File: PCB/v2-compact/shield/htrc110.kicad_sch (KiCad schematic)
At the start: 0 parts

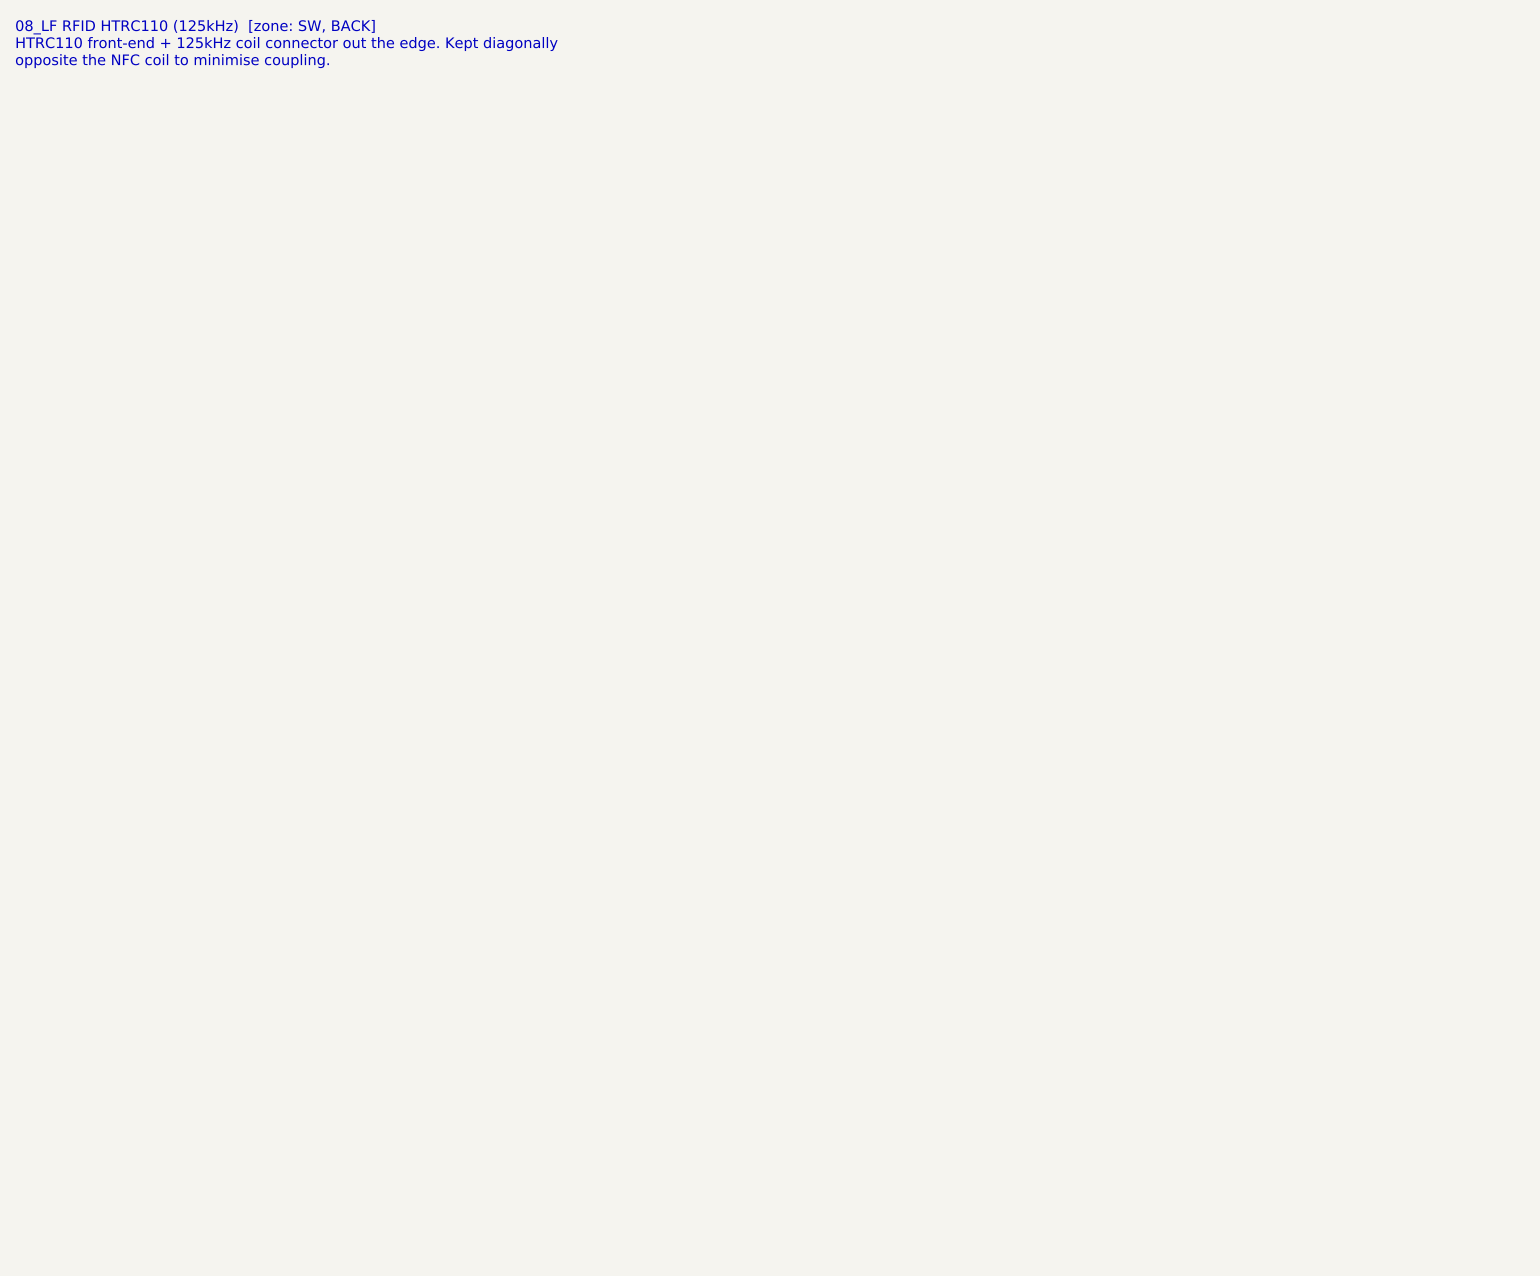
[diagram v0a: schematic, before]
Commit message: Schematics: HTRC110 and RV1106 sheets — full sheet set complete
- 08_LF_RFID_HTRC110: 5V HITAG reader, 3-wire (SCLK/DIN/DOUT) to the C5, DOUT
  open-drain pulled to 3.3V, 4MHz crystal, decoupling. LF coil tank flagged;
  pins 8-14 flagged to verify against the datasheet.
- 04_RV1106_Linux (A3): Core1106 SoM self-powered from its own USB-C (CC
  resistors) with its own microSD; UART to the S3 over J1 (RV_TX/RX/CTRL).
  Symbol is functional with placeholder pin numbers, flagged to verify against
  the Luckfox pinout.
- Add HTRC110 + RV1106 custom symbols to SnowOwl.kicad_sym.

All 17 sheets across both boards are now captured and netlist-verified
(153 nets). Remaining: ERC cleanup (no-connects + power flags), the two flagged
pinouts, RF matching values, and finishing the module footprints.
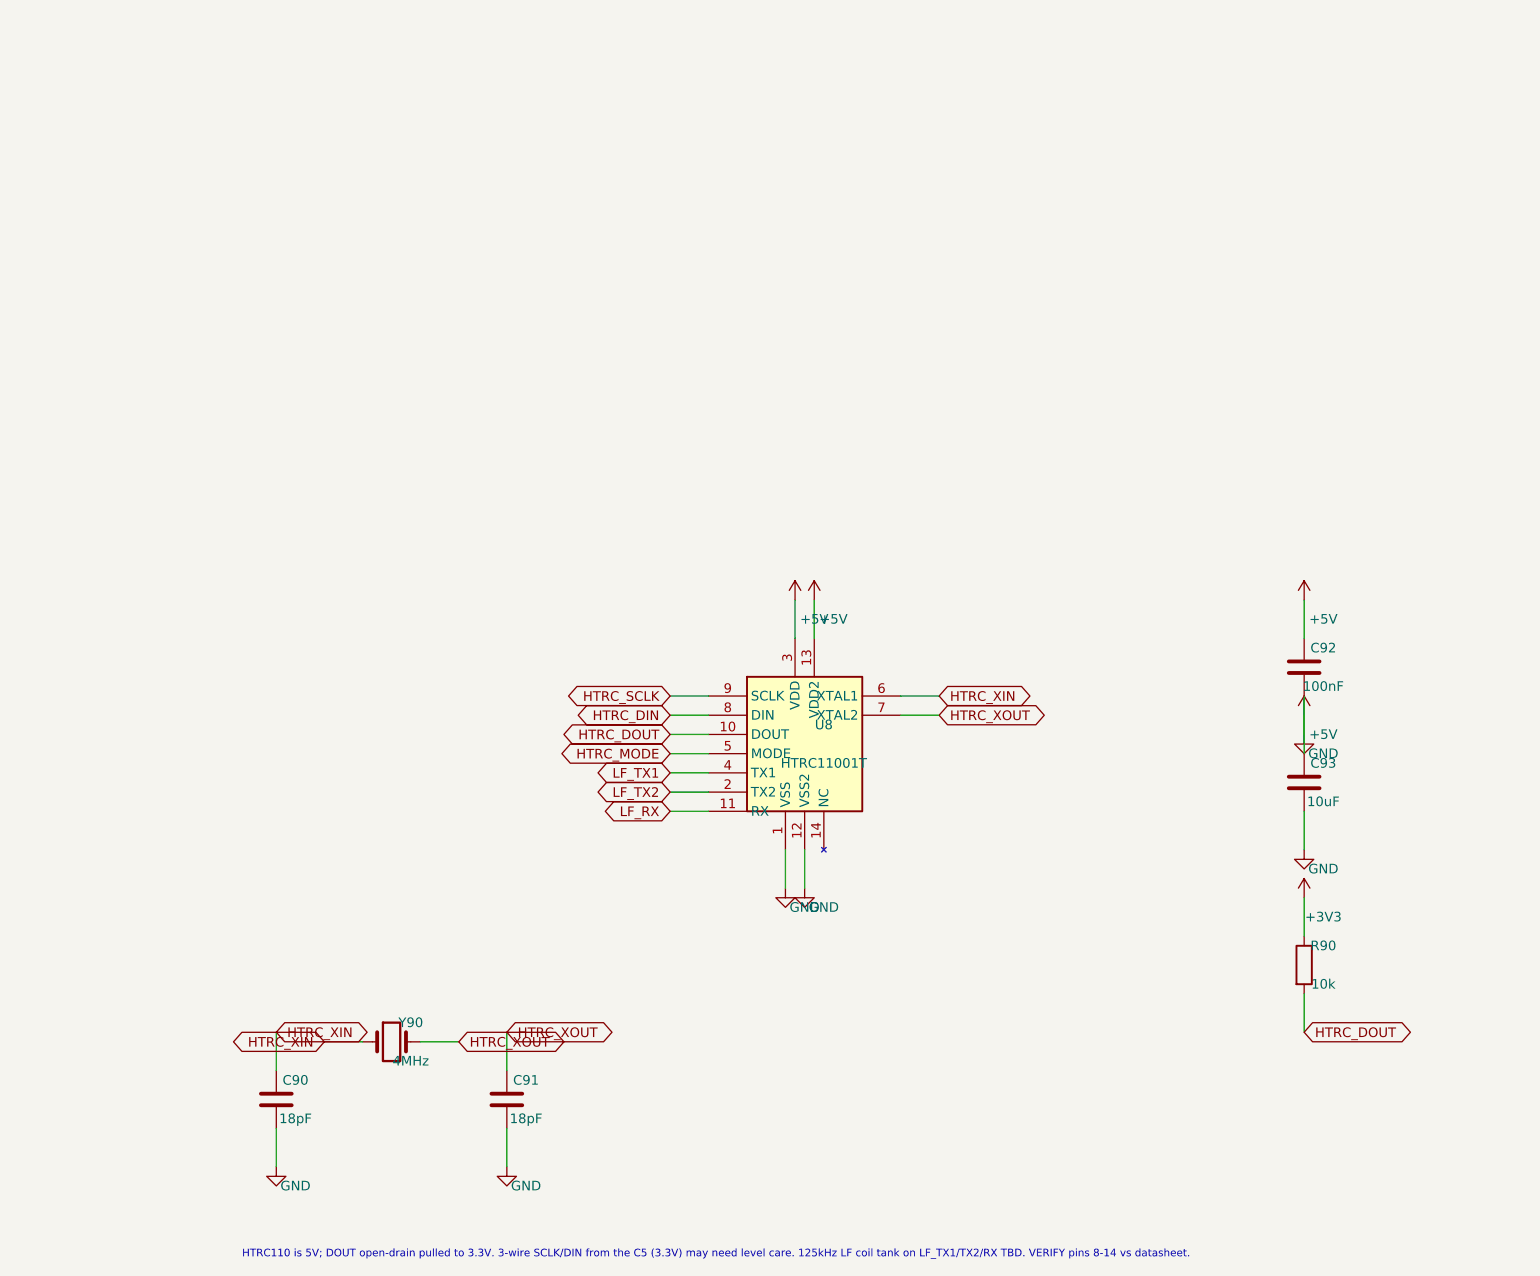
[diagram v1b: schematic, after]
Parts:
- added C90, C91: 18pF, Capacitor_SMD:C_0402_1005Metric, symbol Device:C
- added C92: 100nF, Capacitor_SMD:C_0402_1005Metric, symbol Device:C
- added C93: 10uF, Capacitor_SMD:C_0402_1005Metric, symbol Device:C
- added R90: 10k, Resistor_SMD:R_0402_1005Metric, symbol Device:R
- added U8: HTRC11001T, Package_SO:SO-14_3.9x8.7mm_P1.27mm, symbol SnowOwl:HTRC110
- added Y90: 4MHz, Crystal:Crystal_SMD_3225-4Pin_3.2x2.5mm, symbol Device:Crystal
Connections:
- new net +3V3: R90.1
- new net +5V: C90.2, C91.2, C92.1, C92.2, C93.1, C93.2, U8.1 (VSS), U8.12 (VSS2), U8.13 (VDD2), U8.3 (VDD)
- new net HTRC_DIN: U8.8 (DIN)
- new net HTRC_DOUT: R90.2, U8.10 (DOUT)
- new net HTRC_MODE: U8.5 (MODE)
- new net HTRC_SCLK: U8.9 (SCLK)
- new net HTRC_XIN: C90.1, U8.6 (XTAL1), Y90.1
- new net HTRC_XOUT: C91.1, U8.7 (XTAL2), Y90.2
- new net LF_RX: U8.11 (RX)
- new net LF_TX1: U8.4 (TX1)
- new net LF_TX2: U8.2 (TX2)
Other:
- note added: "HTRC110 is 5V; DOUT open-drain pulled to 3.3V. 3-wire SCLK/DIN from the C5 (3.3V) may need level care. 125kHz LF coil tank on LF_TX1/TX2/RX TBD. VERIFY pins 8-14 vs datasheet."
- note removed: "08_LF RFID HTRC110 (125kHz) [zone: SW, BACK] HTRC110 front-end + 125kHz coil connector out the edge. Kept diagonally opposite the NFC coil to minimise coupling."

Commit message: Schematics: cleanup - HTRC110 footprint (SOIC-14), reset pull-ups (CC1200/GPS), RV1106 power flags
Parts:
- U8: footprint Package_SO:SO-14_3.9x8.7mm_P1.27mm -> Package_SO:SOIC-14_3.9x8.7mm_P1.27mm
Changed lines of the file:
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@@
     (property "Reference" "U8" (at 121.92 107.95 0) (effects (font (size 1.27 1.27))))
     (property "Value" "HTRC11001T" (at 121.92 113.03 0) (effects (font (size 1.27 1.27))))
-    (property "Footprint" "Package_SO:SO-14_3.9x8.7mm_P1.27mm" (at 119.38 110.49 0) (effects (font (size 1.27 1.27)) hide))
+    (property "Footprint" "Package_SO:SOIC-14_3.9x8.7mm_P1.27mm" (at 119.38 110.49 0) (effects (font (size 1.27 1.27)) hide))
     (pin "9")
     (pin "8")
@@
   (symbol (lib_id "power:+5V") (at 118.11 91.44 0) (unit 1)
     (in_bom yes) (on_board yes) (dnp no)
-    (property "Reference" "#PWRF84A393" (at 120.65 88.9 0) (effects (font (size 1.27 1.27)) hide))
+    (property "Reference" "#PWR57BC623" (at 120.65 88.9 0) (effects (font (size 1.27 1.27)) hide))
     (property "Value" "+5V" (at 120.65 93.98 0) (effects (font (size 1.27 1.27))))
     (property "Footprint" "" (at 118.11 91.44 0) (effects (font (size 1.27 1.27)) hide))
     (pin "1")
-    (instances (project "SnowOwl-Shield" (path "/44195f86-bade-400a-b1c6-65bd4a325d72" (reference "#PWRF84A393") (unit 1))))
+    (instances (project "SnowOwl-Shield" (path "/44195f86-bade-400a-b1c6-65bd4a325d72" (reference "#PWR57BC623") (unit 1))))
   )
   (wire (pts (xy 120.65 96.52) (xy 120.65 91.44)) (stroke (width 0) (type default)))
   (symbol (lib_id "power:+5V") (at 120.65 91.44 0) (unit 1)
     (in_bom yes) (on_board yes) (dnp no)
-    (property "Reference" "#PWR5422CC2" (at 123.19 88.9 0) (effects (font (size 1.27 1.27)) hide))
+    (property "Reference" "#PWR49814C8" (at 123.19 88.9 0) (effects (font (size 1.27 1.27)) hide))
     (property "Value" "+5V" (at 123.19 93.98 0) (effects (font (size 1.27 1.27))))
     (property "Footprint" "" (at 120.65 91.44 0) (effects (font (size 1.27 1.27)) hide))
     (pin "1")
-    (instances (project "SnowOwl-Shield" (path "/44195f86-bade-400a-b1c6-65bd4a325d72" (reference "#PWR5422CC2") (unit 1))))
+    (instances (project "SnowOwl-Shield" (path "/44195f86-bade-400a-b1c6-65bd4a325d72" (reference "#PWR49814C8") (unit 1))))
   )
   (wire (pts (xy 116.84 124.46) (xy 116.84 129.54)) (stroke (width 0) (type default)))
   (symbol (lib_id "power:GND") (at 116.84 129.54 0) (unit 1)
     (in_bom yes) (on_board yes) (dnp no)
-    (property "Reference" "#PWR7639A3B" (at 119.38 127 0) (effects (font (size 1.27 1.27)) hide))
+    (property "Reference" "#PWR3B37F8B" (at 119.38 127 0) (effects (font (size 1.27 1.27)) hide))
     (property "Value" "GND" (at 119.38 132.08 0) (effects (font (size 1.27 1.27))))
     (property "Footprint" "" (at 116.84 129.54 0) (effects (font (size 1.27 1.27)) hide))
     (pin "1")
-    (instances (project "SnowOwl-Shield" (path "/44195f86-bade-400a-b1c6-65bd4a325d72" (reference "#PWR7639A3B") (unit 1))))
+    (instances (project "SnowOwl-Shield" (path "/44195f86-bade-400a-b1c6-65bd4a325d72" (reference "#PWR3B37F8B") (unit 1))))
   )
   (wire (pts (xy 119.38 124.46) (xy 119.38 129.54)) (stroke (width 0) (type default)))
   (symbol (lib_id "power:GND") (at 119.38 129.54 0) (unit 1)
     (in_bom yes) (on_board yes) (dnp no)
-    (property "Reference" "#PWRC1F4483" (at 121.92 127 0) (effects (font (size 1.27 1.27)) hide))
+    (property "Reference" "#PWRA2B0F19" (at 121.92 127 0) (effects (font (size 1.27 1.27)) hide))
     (property "Value" "GND" (at 121.92 132.08 0) (effects (font (size 1.27 1.27))))
     (property "Footprint" "" (at 119.38 129.54 0) (effects (font (size 1.27 1.27)) hide))
     (pin "1")
-    (instances (project "SnowOwl-Shield" (path "/44195f86-bade-400a-b1c6-65bd4a325d72" (reference "#PWRC1F4483") (unit 1))))
+    (instances (project "SnowOwl-Shield" (path "/44195f86-bade-400a-b1c6-65bd4a325d72" (reference "#PWRA2B0F19") (unit 1))))
   )
   (symbol (lib_id "Device:Crystal") (at 64.77 149.86 0) (unit 1)
@@
   (symbol (lib_id "power:GND") (at 49.53 166.37 0) (unit 1)
     (in_bom yes) (on_board yes) (dnp no)
-    (property "Reference" "#PWR69757A2" (at 52.07 163.83 0) (effects (font (size 1.27 1.27)) hide))
+    (property "Reference" "#PWR4014A64" (at 52.07 163.83 0) (effects (font (size 1.27 1.27)) hide))
     (property "Value" "GND" (at 52.07 168.91 0) (effects (font (size 1.27 1.27))))
     (property "Footprint" "" (at 49.53 166.37 0) (effects (font (size 1.27 1.27)) hide))
     (pin "1")
-    (instances (project "SnowOwl-Shield" (path "/44195f86-bade-400a-b1c6-65bd4a325d72" (reference "#PWR69757A2") (unit 1))))
+    (instances (project "SnowOwl-Shield" (path "/44195f86-bade-400a-b1c6-65bd4a325d72" (reference "#PWR4014A64") (unit 1))))
   )
   (symbol (lib_id "Device:C") (at 80.01 157.48 0) (unit 1)
@@
   (symbol (lib_id "power:GND") (at 80.01 166.37 0) (unit 1)
     (in_bom yes) (on_board yes) (dnp no)
-    (property "Reference" "#PWRE258DD7" (at 82.55 163.83 0) (effects (font (size 1.27 1.27)) hide))
+    (property "Reference" "#PWR93BA09D" (at 82.55 163.83 0) (effects (font (size 1.27 1.27)) hide))
     (property "Value" "GND" (at 82.55 168.91 0) (effects (font (size 1.27 1.27))))
     (property "Footprint" "" (at 80.01 166.37 0) (effects (font (size 1.27 1.27)) hide))
     (pin "1")
-    (instances (project "SnowOwl-Shield" (path "/44195f86-bade-400a-b1c6-65bd4a325d72" (reference "#PWRE258DD7") (unit 1))))
+    (instances (project "SnowOwl-Shield" (path "/44195f86-bade-400a-b1c6-65bd4a325d72" (reference "#PWR93BA09D") (unit 1))))
   )
   (symbol (lib_id "Device:C") (at 185.42 100.33 0) (unit 1)
@@
   (symbol (lib_id "power:+5V") (at 185.42 91.44 0) (unit 1)
     (in_bom yes) (on_board yes) (dnp no)
-    (property "Reference" "#PWR30B3E4C" (at 187.96 88.9 0) (effects (font (size 1.27 1.27)) hide))
+    (property "Reference" "#PWR6CCB33C" (at 187.96 88.9 0) (effects (font (size 1.27 1.27)) hide))
     (property "Value" "+5V" (at 187.96 93.98 0) (effects (font (size 1.27 1.27))))
     (property "Footprint" "" (at 185.42 91.44 0) (effects (font (size 1.27 1.27)) hide))
     (pin "1")
-    (instances (project "SnowOwl-Shield" (path "/44195f86-bade-400a-b1c6-65bd4a325d72" (reference "#PWR30B3E4C") (unit 1))))
+    (instances (project "SnowOwl-Shield" (path "/44195f86-bade-400a-b1c6-65bd4a325d72" (reference "#PWR6CCB33C") (unit 1))))
   )
   (wire (pts (xy 185.42 104.14) (xy 185.42 109.22)) (stroke (width 0) (type default)))
   (symbol (lib_id "power:GND") (at 185.42 109.22 0) (unit 1)
     (in_bom yes) (on_board yes) (dnp no)
-    (property "Reference" "#PWR708FD7F" (at 187.96 106.68 0) (effects (font (size 1.27 1.27)) hide))
+    (property "Reference" "#PWRB0B70CD" (at 187.96 106.68 0) (effects (font (size 1.27 1.27)) hide))
     (property "Value" "GND" (at 187.96 111.76 0) (effects (font (size 1.27 1.27))))
     (property "Footprint" "" (at 185.42 109.22 0) (effects (font (size 1.27 1.27)) hide))
     (pin "1")
-    (instances (project "SnowOwl-Shield" (path "/44195f86-bade-400a-b1c6-65bd4a325d72" (reference "#PWR708FD7F") (unit 1))))
+    (instances (project "SnowOwl-Shield" (path "/44195f86-bade-400a-b1c6-65bd4a325d72" (reference "#PWRB0B70CD") (unit 1))))
   )
   (symbol (lib_id "Device:C") (at 185.42 115.57 0) (unit 1)
@@
   (symbol (lib_id "power:+5V") (at 185.42 106.68 0) (unit 1)
     (in_bom yes) (on_board yes) (dnp no)
-    (property "Reference" "#PWR9636F1C" (at 187.96 104.14 0) (effects (font (size 1.27 1.27)) hide))
+    (property "Reference" "#PWRE868CCD" (at 187.96 104.14 0) (effects (font (size 1.27 1.27)) hide))
     (property "Value" "+5V" (at 187.96 109.22 0) (effects (font (size 1.27 1.27))))
     (property "Footprint" "" (at 185.42 106.68 0) (effects (font (size 1.27 1.27)) hide))
     (pin "1")
-    (instances (project "SnowOwl-Shield" (path "/44195f86-bade-400a-b1c6-65bd4a325d72" (reference "#PWR9636F1C") (unit 1))))
+    (instances (project "SnowOwl-Shield" (path "/44195f86-bade-400a-b1c6-65bd4a325d72" (reference "#PWRE868CCD") (unit 1))))
   )
   (wire (pts (xy 185.42 119.38) (xy 185.42 124.46)) (stroke (width 0) (type default)))
   (symbol (lib_id "power:GND") (at 185.42 124.46 0) (unit 1)
     (in_bom yes) (on_board yes) (dnp no)
-    (property "Reference" "#PWR34D1786" (at 187.96 121.92 0) (effects (font (size 1.27 1.27)) hide))
+    (property "Reference" "#PWRE559253" (at 187.96 121.92 0) (effects (font (size 1.27 1.27)) hide))
     (property "Value" "GND" (at 187.96 127 0) (effects (font (size 1.27 1.27))))
     (property "Footprint" "" (at 185.42 124.46 0) (effects (font (size 1.27 1.27)) hide))
     (pin "1")
-    (instances (project "SnowOwl-Shield" (path "/44195f86-bade-400a-b1c6-65bd4a325d72" (reference "#PWR34D1786") (unit 1))))
+    (instances (project "SnowOwl-Shield" (path "/44195f86-bade-400a-b1c6-65bd4a325d72" (reference "#PWRE559253") (unit 1))))
   )
   (symbol (lib_id "Device:R") (at 185.42 139.7 0) (unit 1)
@@
   (symbol (lib_id "power:+3V3") (at 185.42 130.81 0) (unit 1)
     (in_bom yes) (on_board yes) (dnp no)
-    (property "Reference" "#PWR839D7E2" (at 187.96 128.27 0) (effects (font (size 1.27 1.27)) hide))
+    (property "Reference" "#PWR2E312E3" (at 187.96 128.27 0) (effects (font (size 1.27 1.27)) hide))
     (property "Value" "+3V3" (at 187.96 133.35 0) (effects (font (size 1.27 1.27))))
     (property "Footprint" "" (at 185.42 130.81 0) (effects (font (size 1.27 1.27)) hide))
     (pin "1")
-    (instances (project "SnowOwl-Shield" (path "/44195f86-bade-400a-b1c6-65bd4a325d72" (reference "#PWR839D7E2") (unit 1))))
+    (instances (project "SnowOwl-Shield" (path "/44195f86-bade-400a-b1c6-65bd4a325d72" (reference "#PWR2E312E3") (unit 1))))
   )
   (wire (pts (xy 185.42 143.51) (xy 185.42 148.59)) (stroke (width 0) (type default)))
